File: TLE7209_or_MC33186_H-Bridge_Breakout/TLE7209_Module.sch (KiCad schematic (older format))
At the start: 10 parts, among them J1 Conn_02x06_Odd_Even, J3 Conn_01x01, U1 TLE7209-2R

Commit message: progress
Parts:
- added R4, R5: 10K, Resistor_SMD:R_0805_2012Metric_Pad1.15x1.40mm_HandSolder, symbol Device:R
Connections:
- net 5V: now also R4.2
- net DIS: now also R5.2
- net EN: now also R4.1
- net GND: now also R5.1
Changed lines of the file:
@@
 Wire Wire Line
 	6700 3550 5950 3550
-Wire Wire Line
-	6700 3750 5950 3750
-Wire Wire Line
-	6700 3900 5950 3900
 $Comp
 L power:GND #PWR0106
@@
 	1    0    0    -1
 $EndComp
+$Comp
+L Device:R R?
+U 1 1 5CC38B64
+P 5250 3750
+AR Path="/5C754D7C/5C75764C" Ref="R?"  Part="1"
+AR Path="/5C754D7C/5CC38B64" Ref="R?"  Part="1"
+AR Path="/5CC38B64" Ref="R4"  Part="1"
+F 0 "R4" H 5250 3900 50  0000 L CNN
+F 1 "10K" V 5250 3750 50  0000 C CNN
+F 2 "Resistor_SMD:R_0805_2012Metric_Pad1.15x1.40mm_HandSolder" H 5250 3750 50  0001 C CNN
+F 3 "~" H 5250 3750 50  0001 C CNN
+F 4 "MOUSER" H 50  850 50  0001 C CNN "VEND"
+	1    5250 3750
+	0    1    1    0
+$EndComp
+Wire Wire Line
+	5400 3750 6700 3750
+$Comp
+L Device:R R?
+U 1 1 5CC3BCBC
+P 5800 4100
+AR Path="/5C754D7C/5C75764C" Ref="R?"  Part="1"
+AR Path="/5C754D7C/5CC3BCBC" Ref="R?"  Part="1"
+AR Path="/5CC3BCBC" Ref="R5"  Part="1"
+F 0 "R5" H 5800 4250 50  0000 L CNN
+F 1 "10K" V 5800 4100 50  0000 C CNN
+F 2 "Resistor_SMD:R_0805_2012Metric_Pad1.15x1.40mm_HandSolder" H 5800 4100 50  0001 C CNN
+F 3 "~" H 5800 4100 50  0001 C CNN
+F 4 "MOUSER" H 600 1200 50  0001 C CNN "VEND"
+	1    5800 4100
+	-1   0    0    1
+$EndComp
+Wire Wire Line
+	5800 3950 5800 3900
+Wire Wire Line
+	5800 3900 6700 3900
+Text Label 4950 3750 0    60   ~ 12
+5V
+Wire Wire Line
+	5100 3750 4950 3750
+$Comp
+L power:GND #PWR?
+U 1 1 5CC41F47
+P 5800 4250
+F 0 "#PWR?" H 5800 4000 50  0001 C CNN
+F 1 "GND" H 5805 4077 50  0000 C CNN
+F 2 "" H 5800 4250 50  0001 C CNN
+F 3 "" H 5800 4250 50  0001 C CNN
+	1    5800 4250
+	1    0    0    -1
+$EndComp

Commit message: sync
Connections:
- net DIS: now also J1.10 (Pin_10); no longer J1.7 (Pin_7)
- net IN2: now also J1.7 (Pin_7); no longer J1.10 (Pin_10)
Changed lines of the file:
@@
 Text Label 9200 1600 0    60   ~ 12
 IN1
-Text Label 9200 1800 0    60   ~ 12
+Text Label 8700 1700 2    60   ~ 12
 IN2
 Text Label 8700 1800 2    60   ~ 12
 EN
-Text Label 8700 1700 2    60   ~ 12
+Text Label 9200 1800 0    60   ~ 12
 DIS
 Text Label 4750 2550 0    60   ~ 12
@@
 	5100 3750 4950 3750
 $Comp
-L power:GND #PWR?
+L power:GND #PWR0108
 U 1 1 5CC41F47
 P 5800 4250
-F 0 "#PWR?" H 5800 4000 50  0001 C CNN
+F 0 "#PWR0108" H 5800 4000 50  0001 C CNN
 F 1 "GND" H 5805 4077 50  0000 C CNN
 F 2 "" H 5800 4250 50  0001 C CNN

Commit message: new try, with IBOM
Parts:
- C1, C2, C3: Manufacturer WURTH -> (none)
- D1: Manufacturer LITTELFUSE -> (none)
- R2, R3, R4, R5: VEND MOUSER -> (none)
- U1: symbol TLE7209_Module-rescue:TLE7209-2R-BOSCH_154_PIN -> TLE7209-2R:TLE7209-2R
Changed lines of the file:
@@
 F 2 "Capacitor_SMD:C_0805_2012Metric_Pad1.15x1.40mm_HandSolder" H 7300 2050 50  0001 C CNN
 F 3 "~" H 7300 2050 50  0001 C CNN
-F 4 "WURTH" H 2350 -850 50  0001 C CNN "Manufacturer"
-F 5 "885012008026" H 2350 -850 50  0001 C CNN "Part #"
-F 6 "MOUSER" H 2350 -850 50  0001 C CNN "VEND"
-F 7 "710-885012008026" H 2350 -850 50  0001 C CNN "VEND#"
+F 4 "885012008026" H 2350 -850 50  0001 C CNN "Part #"
+F 5 "MOUSER" H 2350 -850 50  0001 C CNN "VEND"
+F 6 "710-885012008026" H 2350 -850 50  0001 C CNN "VEND#"
 	1    7300 2050
 	1    0    0    -1
@@
 F 2 "Resistor_SMD:R_0805_2012Metric_Pad1.15x1.40mm_HandSolder" H 7550 2050 50  0001 C CNN
 F 3 "~" H 7550 2050 50  0001 C CNN
-F 4 "MOUSER" H 2350 -850 50  0001 C CNN "VEND"
 	1    7550 2050
 	1    0    0    -1
@@
 F 2 "Resistor_SMD:R_0805_2012Metric_Pad1.15x1.40mm_HandSolder" H 8200 3550 50  0001 C CNN
 F 3 "~" H 8200 3550 50  0001 C CNN
-F 4 "MOUSER" H 2900 0   50  0001 C CNN "VEND"
 	1    8200 3550
 	1    0    0    -1
@@
 F 2 "Capacitor_SMD:C_0805_2012Metric_Pad1.15x1.40mm_HandSolder" H 8500 3550 50  0001 C CNN
 F 3 "~" H 8500 3550 50  0001 C CNN
-F 4 "WURTH" H 2900 0   50  0001 C CNN "Manufacturer"
-F 5 "885012208052" H 2900 0   50  0001 C CNN "Part #"
-F 6 "MOUSER" H 2900 0   50  0001 C CNN "VEND"
-F 7 "710-885012208052" H 2900 0   50  0001 C CNN "VEND#"
+F 4 "885012208052" H 2900 0   50  0001 C CNN "Part #"
+F 5 "MOUSER" H 2900 0   50  0001 C CNN "VEND"
+F 6 "710-885012208052" H 2900 0   50  0001 C CNN "VEND#"
 	1    8500 3550
 	1    0    0    -1
 $EndComp
 $Comp
-L TLE7209_Module-rescue:TLE7209-2R-BOSCH_154_PIN U1
+L TLE7209-2R:TLE7209-2R U1
 U 1 1 5C65688D
 P 7550 1500
@@
 F 2 "Capacitor_SMD:C_0805_2012Metric_Pad1.15x1.40mm_HandSolder" H 3450 2700 50  0001 C CNN
 F 3 "~" H 3450 2700 50  0001 C CNN
-F 4 "WURTH" H -1500 -200 50  0001 C CNN "Manufacturer"
-F 5 "885012008026" H -1500 -200 50  0001 C CNN "Part #"
-F 6 "MOUSER" H -1500 -200 50  0001 C CNN "VEND"
-F 7 "710-885012008026" H -1500 -200 50  0001 C CNN "VEND#"
+F 4 "885012008026" H -1500 -200 50  0001 C CNN "Part #"
+F 5 "MOUSER" H -1500 -200 50  0001 C CNN "VEND"
+F 6 "710-885012008026" H -1500 -200 50  0001 C CNN "VEND#"
 	1    3450 2700
 	1    0    0    -1
@@
 F 6 "MOUSER" H 50  -2450 50  0001 C CNN "VEND"
 F 7 "576-TPSMB24A" H 50  -2450 50  0001 C CNN "VEND#"
-F 8 "LITTELFUSE" H 50  -2450 50  0001 C CNN "Manufacturer"
 	1    2500 2700
 	0    1    1    0
@@
 Wire Wire Line
 	4550 3050 4750 3050
-Wire Wire Line
-	6250 2500 7250 2500
 Wire Wire Line
 	4750 2950 4750 3050
@@
 	1    0    0    -1
 $EndComp
-Connection ~ 7250 2500
-Wire Wire Line
-	7250 2500 7400 2500
 Text Label 9200 2100 0    60   ~ 12
 GND
@@
 F 2 "Resistor_SMD:R_0805_2012Metric_Pad1.15x1.40mm_HandSolder" H 5250 3750 50  0001 C CNN
 F 3 "~" H 5250 3750 50  0001 C CNN
-F 4 "MOUSER" H 50  850 50  0001 C CNN "VEND"
 	1    5250 3750
 	0    1    1    0
@@
 F 2 "Resistor_SMD:R_0805_2012Metric_Pad1.15x1.40mm_HandSolder" H 5800 4100 50  0001 C CNN
 F 3 "~" H 5800 4100 50  0001 C CNN
-F 4 "MOUSER" H 600 1200 50  0001 C CNN "VEND"
 	1    5800 4100
 	-1   0    0    1
@@
 	1    0    0    -1
 $EndComp
+Wire Wire Line
+	6250 2500 7250 2500
+Connection ~ 7250 2500
+Wire Wire Line
+	7250 2500 7400 2500
 $EndSCHEMATC

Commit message: Small update
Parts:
- added C?: CP1, Capacitor_SMD:CP_Elec_8x10, symbol Device:CP1
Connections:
- net 12V: now also C1.1, C2.1, D1.1 (K), R2.1, U1.16 (Vss), U1.5 (Vss), C?.1; no longer C1.2, D1.2 (A)
- net GND: now also C1.2, D1.2 (A), C?.2
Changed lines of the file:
@@
 	4750 2650 4750 2550
 Wire Wire Line
-	2500 3100 3450 3100
+	2500 3100 3000 3100
 Wire Wire Line
-	2500 1900 3450 1900
+	2500 1900 3000 1900
 Text Label 8700 3300 0    60   ~ 12
 OUT1
@@
 Text Label 8700 1500 2    60   ~ 12
 OUT2
-Text Label 3000 3100 0    60   ~ 12
+Text Label 2675 1900 0    60   ~ 12
 12V
 Text Label 9200 1900 0    60   ~ 12
@@
 Wire Wire Line
 	7250 2500 7400 2500
+$Comp
+L power:GND #PWR?
+U 1 1 5E1959D7
+P 3000 3100
+F 0 "#PWR?" H 3000 2850 50  0001 C CNN
+F 1 "GND" H 3005 2927 50  0000 C CNN
+F 2 "" H 3000 3100 50  0001 C CNN
+F 3 "" H 3000 3100 50  0001 C CNN
+	1    3000 3100
+	1    0    0    -1
+$EndComp
+$Comp
+L Device:CP1 C?
+U 1 1 5E196218
+P 3000 2675
+F 0 "C?" H 3115 2721 50  0000 L CNN
+F 1 "CP1" H 3115 2630 50  0000 L CNN
+F 2 "Capacitor_SMD:CP_Elec_8x10" H 3000 2675 50  0001 C CNN
+F 3 "~" H 3000 2675 50  0001 C CNN
+	1    3000 2675
+	1    0    0    -1
+$EndComp
+Wire Wire Line
+	3000 2825 3000 3100
+Connection ~ 3000 3100
+Wire Wire Line
+	3000 3100 3450 3100
+Wire Wire Line
+	3000 2525 3000 1900
+Connection ~ 3000 1900
+Wire Wire Line
+	3000 1900 3450 1900
 $EndSCHEMATC

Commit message: Updated with LSLC Pn
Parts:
- C1: LSLC (none) -> C49678; Part # 885012008026 -> (none); VEND MOUSER -> (none); VEND# 710-885012008026 -> (none)
- C2: LSLC (none) -> C1739; Part # 885012008026 -> (none); VEND MOUSER -> (none); VEND# 710-885012008026 -> (none)
- C3: LSLC (none) -> C1710; Part # 885012208052 -> (none); VEND MOUSER -> (none); VEND# 710-885012208052 -> (none)
- D1: Part # TPSMB24A -> (none); Part Manufacturer Littelfuse -> (none); VEND MOUSER -> (none)
- R1: LSLC (none) -> C17713
- R2: LSLC (none) -> C17514
- R3: LSLC (none) -> C17673
- R4, R5: LSLC (none) -> C17414
- gave numbers to parts that had none: 1
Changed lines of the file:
@@
 F 2 "Capacitor_SMD:C_0805_2012Metric_Pad1.15x1.40mm_HandSolder" H 7300 2050 50  0001 C CNN
 F 3 "~" H 7300 2050 50  0001 C CNN
-F 4 "885012008026" H 2350 -850 50  0001 C CNN "Part #"
-F 5 "MOUSER" H 2350 -850 50  0001 C CNN "VEND"
-F 6 "710-885012008026" H 2350 -850 50  0001 C CNN "VEND#"
+F 4 " C1739" H 0   0   50  0001 C CNN "LSLC"
 	1    7300 2050
 	1    0    0    -1
@@
 F 2 "Resistor_SMD:R_0805_2012Metric_Pad1.15x1.40mm_HandSolder" H 7550 2050 50  0001 C CNN
 F 3 "~" H 7550 2050 50  0001 C CNN
+F 4 " C17514" H 0   0   50  0001 C CNN "LSLC"
 	1    7550 2050
 	1    0    0    -1
@@
 F 2 "Resistor_SMD:R_0805_2012Metric_Pad1.15x1.40mm_HandSolder" H 8200 3550 50  0001 C CNN
 F 3 "~" H 8200 3550 50  0001 C CNN
+F 4 " C17673" H 0   0   50  0001 C CNN "LSLC"
 	1    8200 3550
 	1    0    0    -1
@@
 F 2 "Capacitor_SMD:C_0805_2012Metric_Pad1.15x1.40mm_HandSolder" H 8500 3550 50  0001 C CNN
 F 3 "~" H 8500 3550 50  0001 C CNN
-F 4 "885012208052" H 2900 0   50  0001 C CNN "Part #"
-F 5 "MOUSER" H 2900 0   50  0001 C CNN "VEND"
-F 6 "710-885012208052" H 2900 0   50  0001 C CNN "VEND#"
+F 4 " C1710" H 0   0   50  0001 C CNN "LSLC"
 	1    8500 3550
 	1    0    0    -1
@@
 F 2 "Resistor_SMD:R_0805_2012Metric_Pad1.15x1.40mm_HandSolder" V 4680 2800 30  0001 C CNN
 F 3 "" H 4750 2800 30  0000 C CNN
+F 4 " C17713" H 0   0   50  0001 C CNN "LSLC"
 	1    4750 2800
 	1    0    0    -1
@@
 F 2 "Capacitor_SMD:C_0805_2012Metric_Pad1.15x1.40mm_HandSolder" H 3450 2700 50  0001 C CNN
 F 3 "~" H 3450 2700 50  0001 C CNN
-F 4 "885012008026" H -1500 -200 50  0001 C CNN "Part #"
-F 5 "MOUSER" H -1500 -200 50  0001 C CNN "VEND"
-F 6 "710-885012008026" H -1500 -200 50  0001 C CNN "VEND#"
+F 4 "C49678" H 0   0   50  0001 C CNN "LSLC"
 	1    3450 2700
 	1    0    0    -1
@@
 F 2 "Diode_SMD:D_SMA" H 2500 2500 50  0001 C CNN
 F 3 "https://www.vishay.com/docs/88301/15ke.pdf" H 2450 2700 50  0001 C CNN
-F 4 "TPSMB24A" H 50  -2450 50  0001 C CNN "Part #"
-F 5 "Littelfuse" H 50  -2450 50  0001 C CNN "Part Manufacturer"
-F 6 "MOUSER" H 50  -2450 50  0001 C CNN "VEND"
-F 7 "576-TPSMB24A" H 50  -2450 50  0001 C CNN "VEND#"
+F 4 "576-TPSMB24A" H 50  -2450 50  0001 C CNN "VEND#"
 	1    2500 2700
 	0    1    1    0
@@
 F 2 "Resistor_SMD:R_0805_2012Metric_Pad1.15x1.40mm_HandSolder" H 5250 3750 50  0001 C CNN
 F 3 "~" H 5250 3750 50  0001 C CNN
+F 4 " C17414" H 0   0   50  0001 C CNN "LSLC"
 	1    5250 3750
 	0    1    1    0
@@
 F 2 "Resistor_SMD:R_0805_2012Metric_Pad1.15x1.40mm_HandSolder" H 5800 4100 50  0001 C CNN
 F 3 "~" H 5800 4100 50  0001 C CNN
+F 4 " C17414" H 0   0   50  0001 C CNN "LSLC"
 	1    5800 4100
 	-1   0    0    1
@@
 	7250 2500 7400 2500
 $Comp
-L power:GND #PWR?
+L power:GND #PWR0109
 U 1 1 5E1959D7
 P 3000 3100
-F 0 "#PWR?" H 3000 2850 50  0001 C CNN
+F 0 "#PWR0109" H 3000 2850 50  0001 C CNN
 F 1 "GND" H 3005 2927 50  0000 C CNN
 F 2 "" H 3000 3100 50  0001 C CNN
@@
 $EndComp
 $Comp
-L Device:CP1 C?
+L Device:CP1 C4
 U 1 1 5E196218
 P 3000 2675
-F 0 "C?" H 3115 2721 50  0000 L CNN
+F 0 "C4" H 3115 2721 50  0000 L CNN
 F 1 "CP1" H 3115 2630 50  0000 L CNN
 F 2 "Capacitor_SMD:CP_Elec_8x10" H 3000 2675 50  0001 C CNN

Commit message: Pcb Update
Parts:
- C4: footprint Capacitor_SMD:CP_Elec_8x10 -> Capacitor_SMD:CP_Elec_8x6.7
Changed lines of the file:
@@
 F 0 "C4" H 3115 2721 50  0000 L CNN
 F 1 "CP1" H 3115 2630 50  0000 L CNN
-F 2 "Capacitor_SMD:CP_Elec_8x10" H 3000 2675 50  0001 C CNN
+F 2 "Capacitor_SMD:CP_Elec_8x6.7" H 3000 2675 50  0001 C CNN
 F 3 "~" H 3000 2675 50  0001 C CNN
 	1    3000 2675

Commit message: version (#27)
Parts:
- C4: footprint Capacitor_SMD:CP_Elec_8x6.7 -> Capacitor_SMD:CP_Elec_8x10
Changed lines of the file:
@@
 encoding utf-8
 Sheet 1 1
-Title ""
+Title "TLE7209 Module"
 Date ""
-Rev ""
+Rev "0.2"
 Comp ""
 Comment1 ""
@@
 F 0 "C4" H 3115 2721 50  0000 L CNN
 F 1 "CP1" H 3115 2630 50  0000 L CNN
-F 2 "Capacitor_SMD:CP_Elec_8x6.7" H 3000 2675 50  0001 C CNN
+F 2 "Capacitor_SMD:CP_Elec_8x10" H 3000 2675 50  0001 C CNN
 F 3 "~" H 3000 2675 50  0001 C CNN
 	1    3000 2675

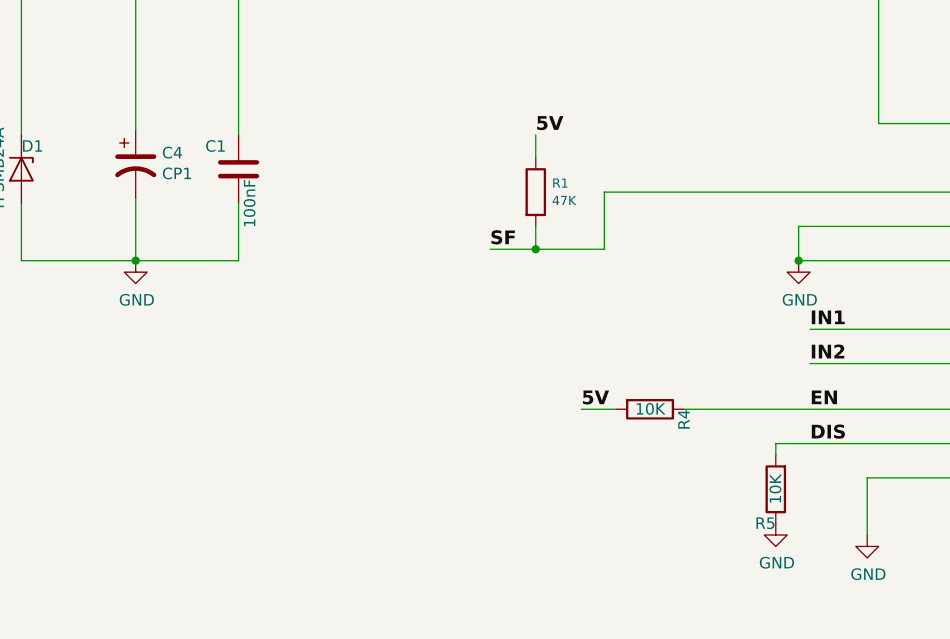
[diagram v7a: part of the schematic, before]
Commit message: C4 value notes 100uf on schematic and PCB silk R4 & R5 now note 2.2K generated schematic PDF as 0.3
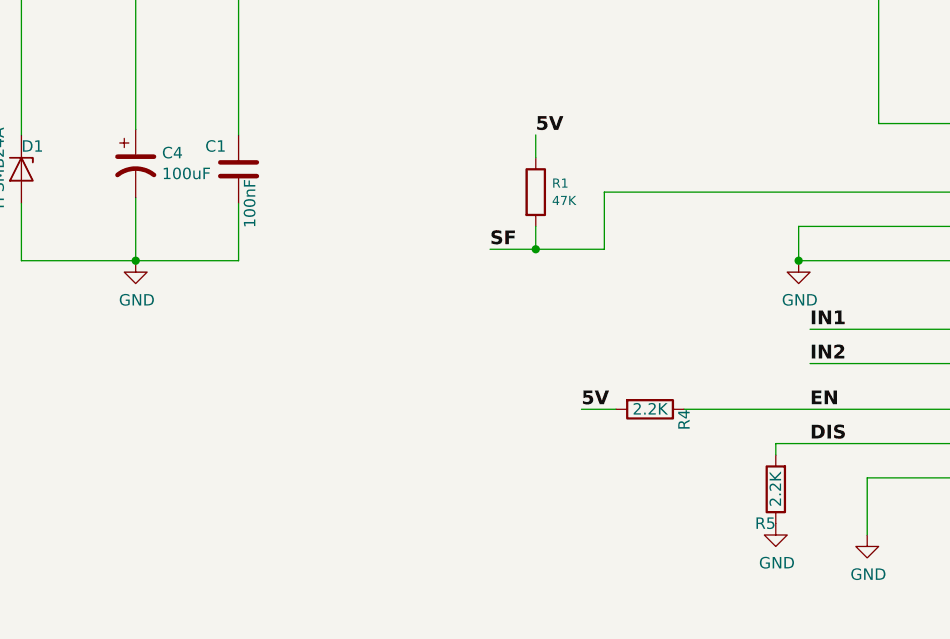
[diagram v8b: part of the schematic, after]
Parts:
- C4: value CP1 -> 100uF
- R4, R5: value 10K -> 2.2K; LSLC C17414 -> C101970
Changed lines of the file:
@@
 EESchema Schematic File Version 4
-LIBS:TLE7209_Module-cache
-EELAYER 29 0
+EELAYER 30 0
 EELAYER END
-$Descr A4 11693 8268
+$Descr A 11000 8500
 encoding utf-8
 Sheet 1 1
 Title "TLE7209 Module"
-Date ""
-Rev "0.2"
-Comp ""
+Date "2020-04-05"
+Rev "0.3"
+Comp "rusEFI"
 Comment1 ""
 Comment2 ""
@@
 AR Path="/5CC38B64" Ref="R4"  Part="1"
 F 0 "R4" H 5250 3900 50  0000 L CNN
-F 1 "10K" V 5250 3750 50  0000 C CNN
+F 1 "2.2K" V 5250 3750 50  0000 C CNN
 F 2 "Resistor_SMD:R_0805_2012Metric_Pad1.15x1.40mm_HandSolder" H 5250 3750 50  0001 C CNN
 F 3 "~" H 5250 3750 50  0001 C CNN
-F 4 " C17414" H 0   0   50  0001 C CNN "LSLC"
+F 4 "C101970" H 0   0   50  0001 C CNN "LSLC"
 	1    5250 3750
 	0    1    1    0
@@
 Wire Wire Line
 	5400 3750 6700 3750
-$Comp
-L Device:R R?
-U 1 1 5CC3BCBC
-P 5800 4100
-AR Path="/5C754D7C/5C75764C" Ref="R?"  Part="1"
-AR Path="/5C754D7C/5CC3BCBC" Ref="R?"  Part="1"
-AR Path="/5CC3BCBC" Ref="R5"  Part="1"
-F 0 "R5" H 5800 4250 50  0000 L CNN
-F 1 "10K" V 5800 4100 50  0000 C CNN
-F 2 "Resistor_SMD:R_0805_2012Metric_Pad1.15x1.40mm_HandSolder" H 5800 4100 50  0001 C CNN
-F 3 "~" H 5800 4100 50  0001 C CNN
-F 4 " C17414" H 0   0   50  0001 C CNN "LSLC"
-	1    5800 4100
-	-1   0    0    1
-$EndComp
 Wire Wire Line
 	5800 3950 5800 3900
@@
 P 3000 2675
 F 0 "C4" H 3115 2721 50  0000 L CNN
-F 1 "CP1" H 3115 2630 50  0000 L CNN
+F 1 "100uF" H 3115 2630 50  0000 L CNN
 F 2 "Capacitor_SMD:CP_Elec_8x10" H 3000 2675 50  0001 C CNN
 F 3 "~" H 3000 2675 50  0001 C CNN
@@
 Wire Wire Line
 	3000 1900 3450 1900
+$Comp
+L Device:R R?
+U 1 1 5CC3BCBC
+P 5800 4100
+AR Path="/5C754D7C/5C75764C" Ref="R?"  Part="1"
+AR Path="/5C754D7C/5CC3BCBC" Ref="R?"  Part="1"
+AR Path="/5CC3BCBC" Ref="R5"  Part="1"
+F 0 "R5" H 5800 4250 50  0000 L CNN
+F 1 "2.2K" V 5800 4100 50  0000 C CNN
+F 2 "Resistor_SMD:R_0805_2012Metric_Pad1.15x1.40mm_HandSolder" H 5800 4100 50  0001 C CNN
+F 3 "~" H 5800 4100 50  0001 C CNN
+F 4 "C101970" H 0   0   50  0001 C CNN "LSLC"
+	1    5800 4100
+	-1   0    0    1
+$EndComp
 $EndSCHEMATC
